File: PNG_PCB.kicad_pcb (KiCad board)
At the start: 2 copper layers, 109 parts, among them J1 screw term, J10 screw term, J11 screw term, J12 screw term, J13 screw term, J14 screw term, J15 screw term, J16 screw term, J17 screw term, J18 screw term, J19 screw term, J2 screw term, J20 screw term, J21 screw term, J22 screw term, J23 screw term, J24 screw term, J25 screw term, J26 screw term, J27 screw term, J28 screw term, J29 screw term, J3 screw term, J30 screw term, J4 screw term, J5 screw term, J6 screw term, J7 screw term, J8 screw term, J9 screw term, U1 Teensy4.1, U2 Mux, U3 MCP6004, U4 Mux, U5 Mux, U6 MCP6004, U7 Mux, U8 Mux, U9 MCP6004

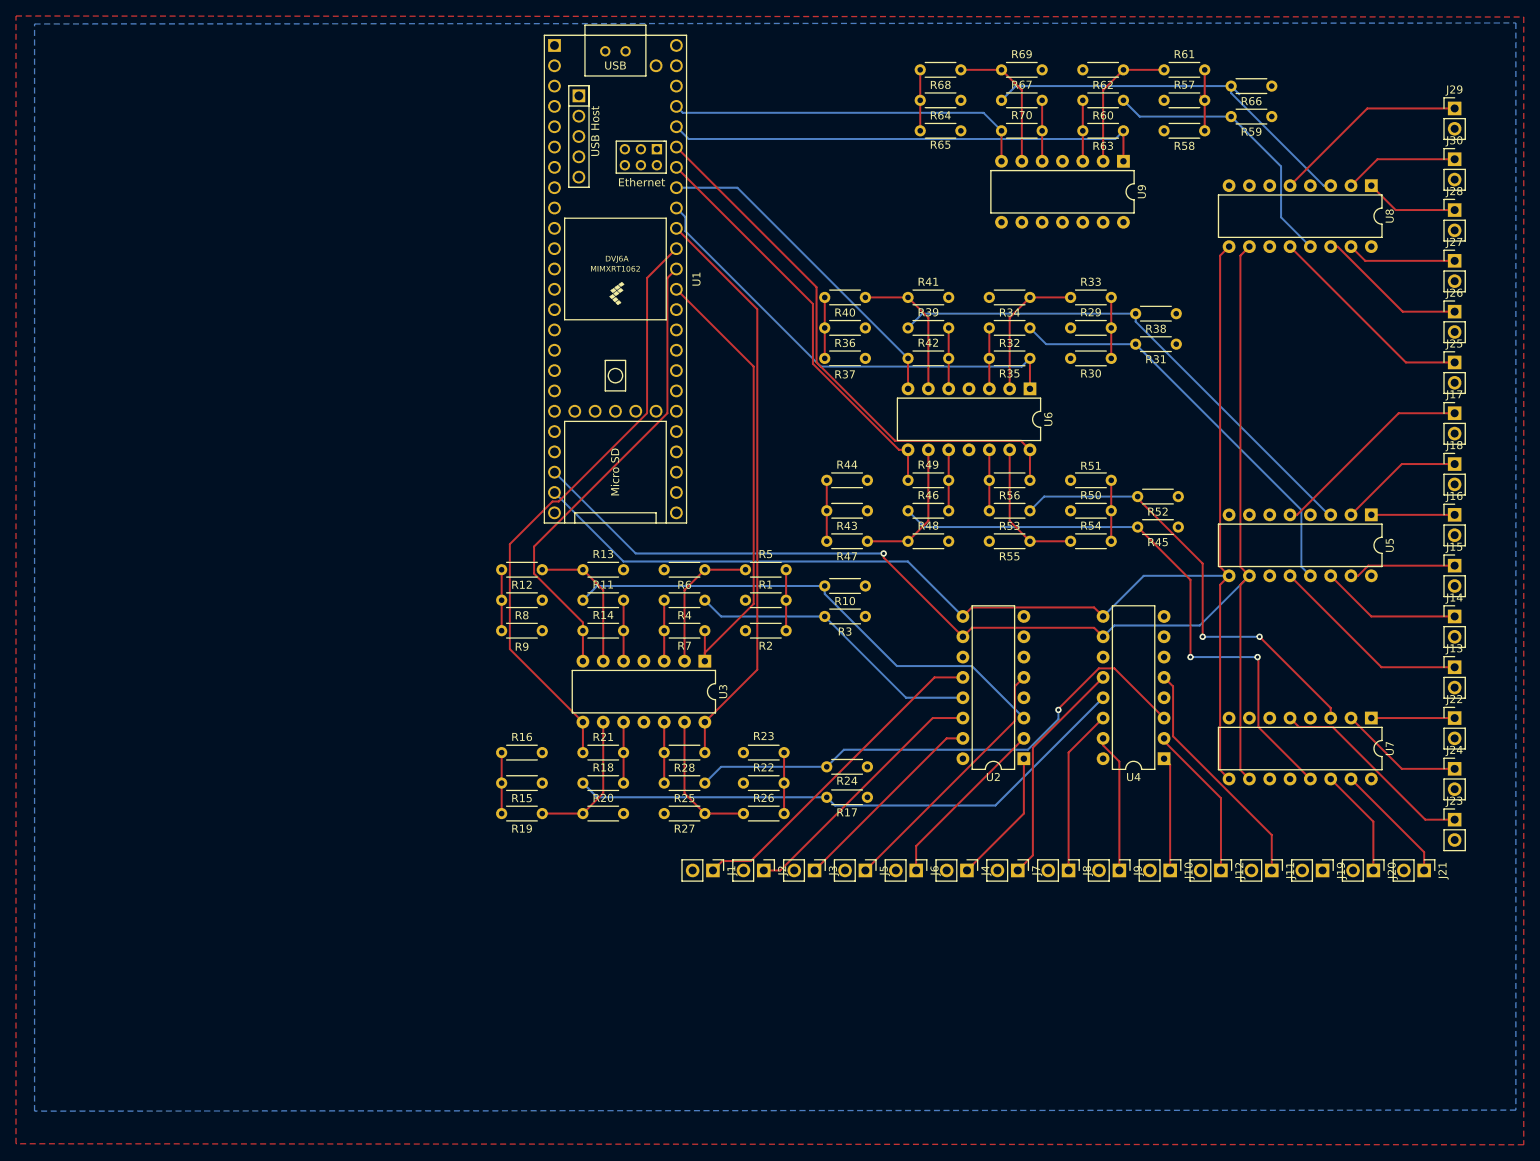
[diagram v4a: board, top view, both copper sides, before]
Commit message: added edge cuts and resized board to minimize footprint
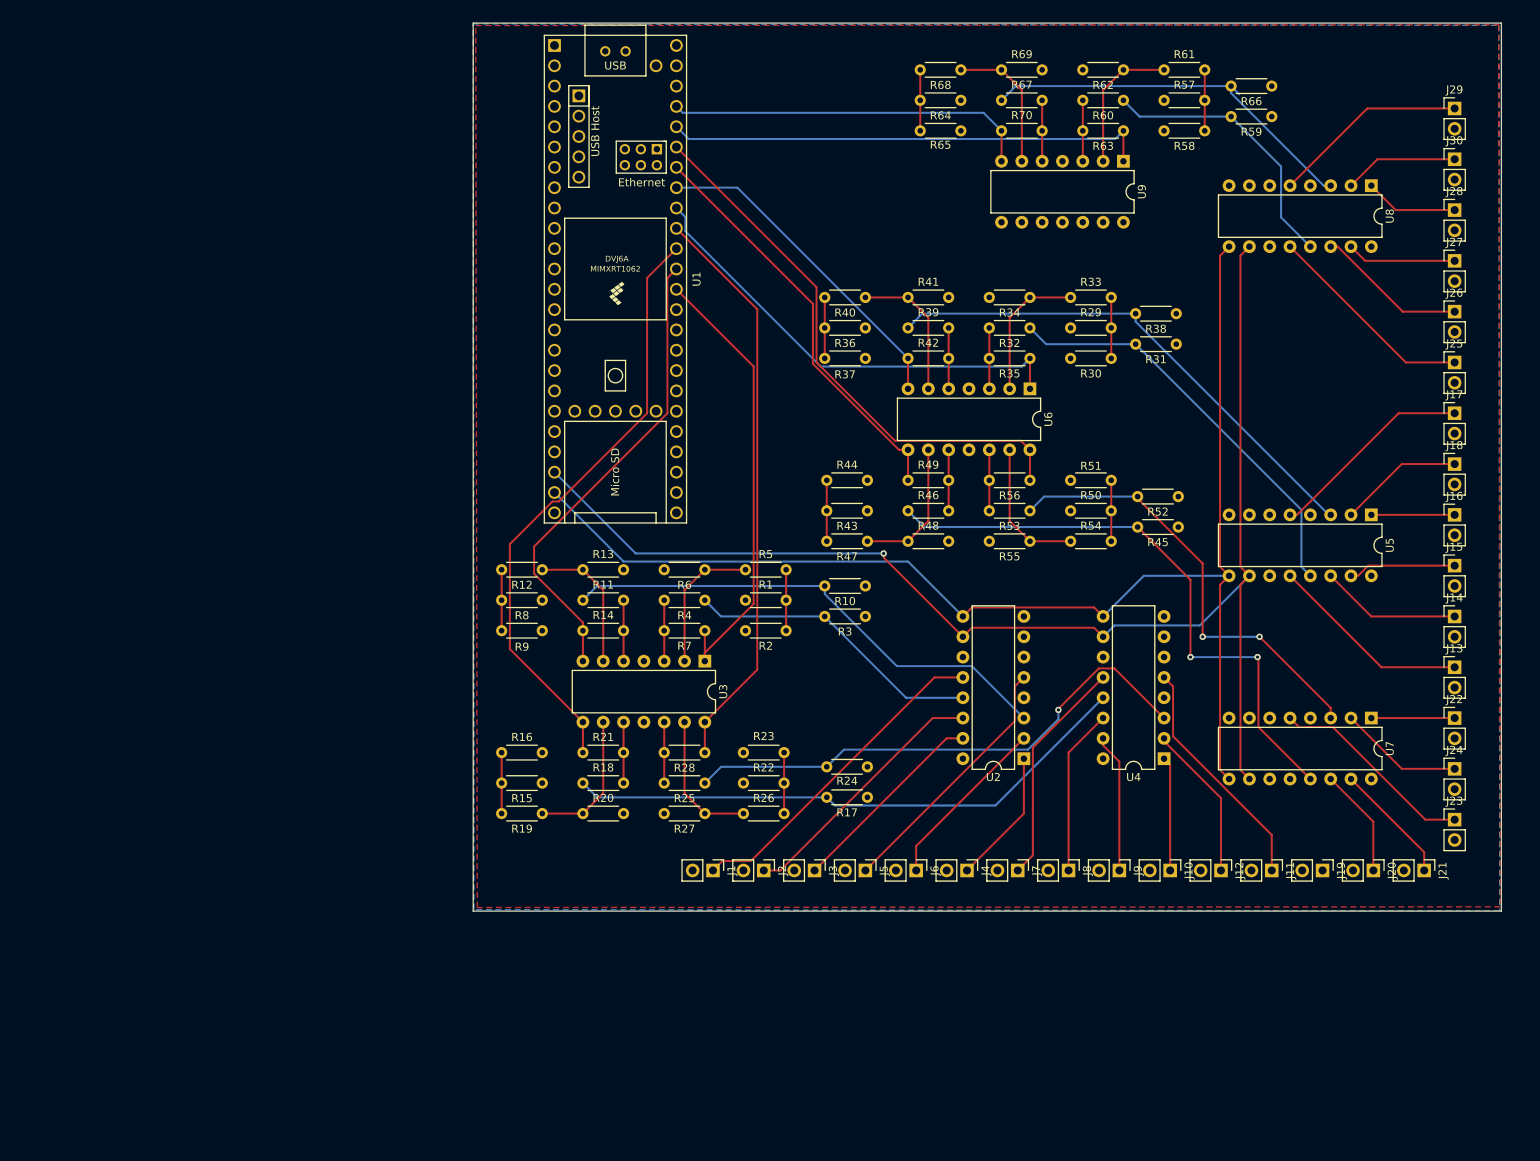
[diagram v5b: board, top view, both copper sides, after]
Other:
- board outline added: 128.5 x 111 mm
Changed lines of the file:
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@@
   (general
     (thickness 1.6)
-    (drawings 0)
+    (drawings 1)
     (tracks 286)
     (zones 0)
@@
     )
   )
+  (gr_poly (pts (xy 258.064 154.94) (xy 129.54 154.94) (xy 129.54 43.942) (xy 258.064 43.942)) (layer Edge.Cuts) (width 0.1))
   (segment (start 160.687001 148.684999) (end 159.512 149.86) (width 0.25) (layer F.Cu) (net 2))
   (segment (start 164.249999 148.684999) (end 160.687001 148.684999) (width 0.25) (layer F.Cu) (net 2))
@@
     (polygon
       (pts
-        (xy 72.39 184.023) (xy 72.39 43.053) (xy 260.858 43.18) (xy 260.858 184.15)
+        (xy 130.048 154.4955) (xy 129.8575 44.243625) (xy 257.7465 44.148375) (xy 257.937 154.40025)
       )
     )
@@
     (polygon
       (pts
-        (xy 74.712349 179.942426) (xy 74.712349 44.052426) (xy 259.878349 43.925426) (xy 259.878349 179.815426)
+        (xy 129.648826 154.7495) (xy 129.54 44.052426) (xy 257.755587 44.219463) (xy 257.864413 154.916537)
       )
     )

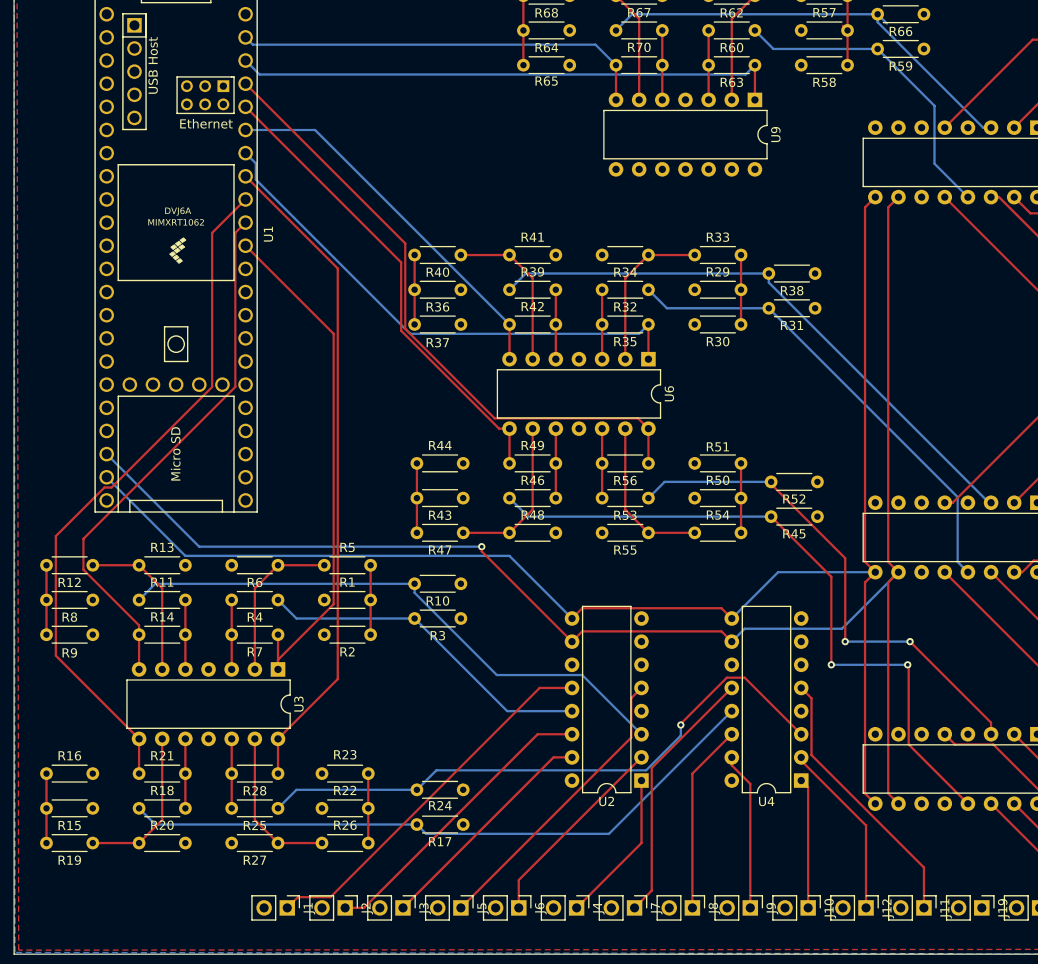
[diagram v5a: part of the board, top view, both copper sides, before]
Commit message: fixed drc errors
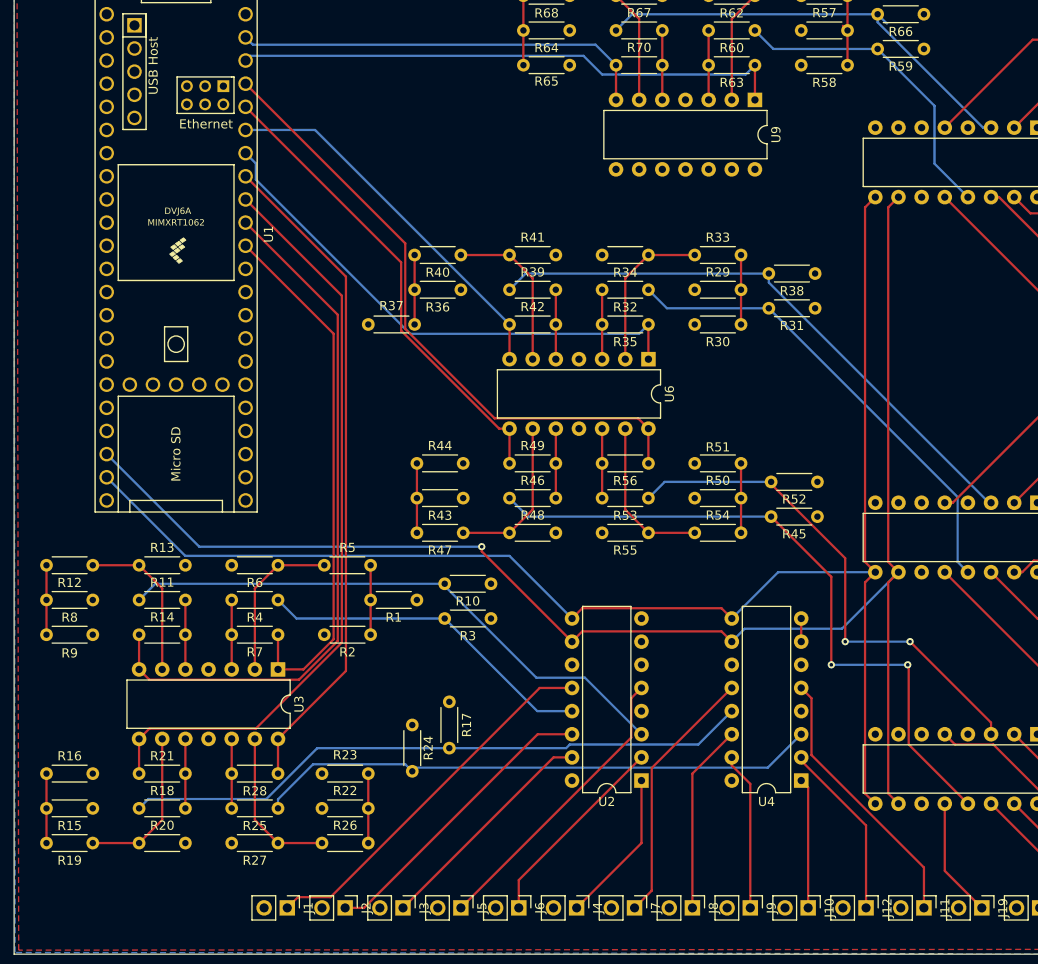
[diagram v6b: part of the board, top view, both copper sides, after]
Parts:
- moved R17 13.5 mm to (177.3, 127.3), turned to 270 degrees
- moved R1 10.2 mm to (173.7, 116.1), turned to 180 degrees
- moved R24 9.04 mm to (173.2, 129.8), turned to 270 degrees
- moved R10 3.30 mm to (181.9, 114.3)
- moved R3 3.30 mm to (181.9, 118.1)
- turned R37 to 180 degrees
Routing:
- net /ADC_IN_1: track 58.9 -> 77.9 mm
- net /ampC1/mux0: track 0.00 -> 13.1 mm
- net /ADC_IN_2: track 75.9 -> 83.4 mm
- net /ampD0/V1: track 66.7 -> 62.0 mm, vias 1 -> 0
- net GND: track 0.00 -> 2.54 mm
- net /ampC0/V1: track 71.8 -> 69.4 mm
- net /ADC_IN_0: track 56.8 -> 58.5 mm
- net /ADC_IN_3: track 72.4 -> 73.2 mm

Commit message: added purdue logo
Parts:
- added G***: LOGO, PNG_PCB:PNG_Logo, F.Cu at (173.5, 67.1)
